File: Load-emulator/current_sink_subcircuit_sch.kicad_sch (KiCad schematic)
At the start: 3 parts, among them Q4 TIP41C, U4 AD8001AN

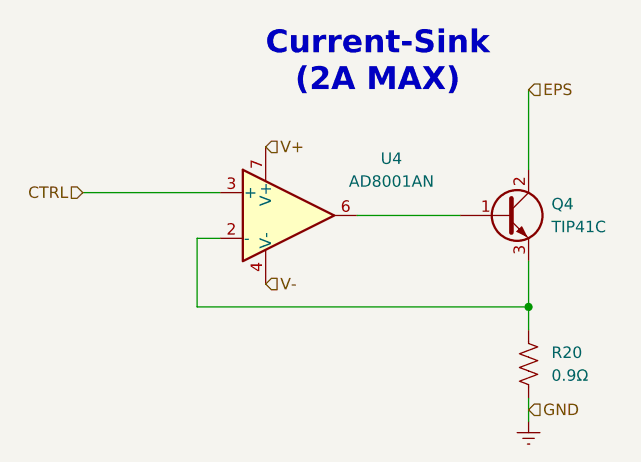
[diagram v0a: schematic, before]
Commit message: Replacement of the microcontroller w/ picoblade
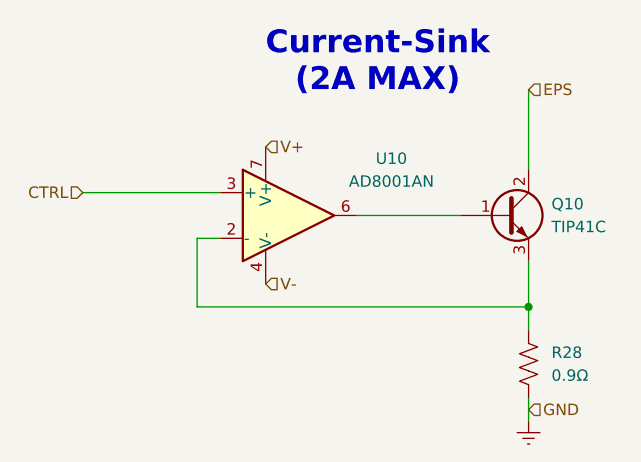
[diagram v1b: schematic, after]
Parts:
- renumbered Q4 to Q10, R20 to R28, U4 to U10
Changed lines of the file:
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@@
 		(dnp no)
 		(fields_autoplaced yes)
-		(property "Reference" "R20"
+		(property "Reference" "R28"
 			(at 167.64 105.4099 0)
 			(effects
@@
 				(path "/9054bfd2-3cc0-4c96-aa71-abdb09b76dc7/a12c045f-372a-4c5b-93d1-0c234b5f9c5c/87a0f9ee-fa92-48a0-98d1-72d297c3468c"
 					(reference "R21")
+					(unit 1)
+				)
+				(path "/9054bfd2-3cc0-4c96-aa71-abdb09b76dc7/a12c045f-372a-4c5b-93d1-0c234b5f9c5c/c40377b4-6929-4e4a-ac2d-4b484617f896"
+					(reference "R35")
 					(unit 1)
 				)
@@
 		(dnp no)
 		(fields_autoplaced yes)
-		(property "Reference" "#PWR033"
+		(property "Reference" "#PWR061"
 			(at 165.1 119.38 0)
 			(effects
@@
 				(path "/9054bfd2-3cc0-4c96-aa71-abdb09b76dc7/a12c045f-372a-4c5b-93d1-0c234b5f9c5c/87a0f9ee-fa92-48a0-98d1-72d297c3468c"
 					(reference "#PWR034")
+					(unit 1)
+				)
+				(path "/9054bfd2-3cc0-4c96-aa71-abdb09b76dc7/a12c045f-372a-4c5b-93d1-0c234b5f9c5c/c40377b4-6929-4e4a-ac2d-4b484617f896"
+					(reference "#PWR0101")
 					(unit 1)
 				)
@@
 		(dnp no)
 		(fields_autoplaced yes)
-		(property "Reference" "Q4"
+		(property "Reference" "Q10"
 			(at 167.64 88.8999 0)
 			(effects
@@
 				(path "/9054bfd2-3cc0-4c96-aa71-abdb09b76dc7/a12c045f-372a-4c5b-93d1-0c234b5f9c5c/87a0f9ee-fa92-48a0-98d1-72d297c3468c"
 					(reference "Q5")
+					(unit 1)
+				)
+				(path "/9054bfd2-3cc0-4c96-aa71-abdb09b76dc7/a12c045f-372a-4c5b-93d1-0c234b5f9c5c/c40377b4-6929-4e4a-ac2d-4b484617f896"
+					(reference "Q13")
 					(unit 1)
 				)
@@
 		(dnp no)
 		(fields_autoplaced yes)
-		(property "Reference" "U4"
+		(property "Reference" "U10"
 			(at 149.86 83.8514 0)
 			(effects
@@
 					(unit 1)
 				)
+				(path "/9054bfd2-3cc0-4c96-aa71-abdb09b76dc7/a12c045f-372a-4c5b-93d1-0c234b5f9c5c/c40377b4-6929-4e4a-ac2d-4b484617f896"
+					(reference "U13")
+					(unit 1)
+				)

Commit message: Added footprints for the remaining resistors, capacitors and ampops, as well as some 3D models
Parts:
- R28: footprint (none) -> Resistor_SMD:R_0201_0603Metric
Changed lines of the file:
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@@
 			)
 		)
-		(property "Footprint" ""
+		(property "Footprint" "Resistor_SMD:R_0201_0603Metric"
 			(at 166.116 106.934 90)
 			(effects

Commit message: Forgot to save files before last commit
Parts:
- removed U10: AD8001AN, Package_DIP:DIP-8_W7.62mm, symbol Amplifier_Operational:AD8001AN
- added U2: LM318H, LM318M:SOIC127P599X175-8N, symbol Amplifier_Operational:LM318H
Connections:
- net CTRL: now also U2.3 (+)
- net V+: now also U2.7 (V+)
- net V-: now also U2.4 (V-)
- net at Q10.3 (E), R28.1: now also U2.2 (-)
- net at Q10.1 (B): now also U2.6
- no-connect marks 0 -> 3
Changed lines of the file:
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@@
 		(color 0 0 0 0)
+	)
+	(no_connect
+		(at 138.43 97.79)
+	)
+	(no_connect
+		(at 138.43 82.55)
+	)
+	(no_connect
+		(at 140.97 97.79)
 	)
 	(wire
@@
 	(hierarchical_label "V+"
 		(shape input)
-		(at 135.89 82.55 0)
+		(at 135.89 82.55 90)
 		(fields_autoplaced yes)
 		(effects
@@
 	(hierarchical_label "V-"
 		(shape input)
-		(at 135.89 97.79 0)
+		(at 135.89 97.79 180)
 		(fields_autoplaced yes)
 		(effects
@@
 				(size 1.27 1.27)
 			)
-			(justify left)
+			(justify right)
 		)
 	)
@@
 	)
 	(symbol
-		(lib_id "Amplifier_Operational:AD8001AN")
+		(lib_id "Amplifier_Operational:LM318H")
 		(at 138.43 90.17 0)
 		(unit 1)
@@
 		(dnp no)
 		(fields_autoplaced yes)
-		(property "Reference" "U10"
-			(at 149.86 83.8514 0)
-			(effects
-				(font
-					(size 1.27 1.27)
-				)
-			)
-		)
-		(property "Value" "AD8001AN"
-			(at 149.86 86.3914 0)
-			(effects
-				(font
-					(size 1.27 1.27)
-				)
-			)
-		)
-		(property "Footprint" "Package_DIP:DIP-8_W7.62mm"
-			(at 135.89 95.25 0)
-			(effects
-				(font
-					(size 1.27 1.27)
-				)
-				(justify left)
-				(hide yes)
-			)
-		)
-		(property "Datasheet" "https://www.analog.com/media/en/technical-documentation/data-sheets/ad8001.pdf"
-			(at 142.24 86.36 0)
-			(effects
-				(font
-					(size 1.27 1.27)
-				)
-				(hide yes)
-			)
-		)
-		(property "Description" "Current Feedback Amplifier, 800 MHz, 50mW, DIP-8"
+		(property "Reference" "U2"
+			(at 148.59 83.8514 0)
+			(effects
+				(font
+					(size 1.27 1.27)
+				)
+			)
+		)
+		(property "Value" "LM318H"
+			(at 148.59 86.3914 0)
+			(effects
+				(font
+					(size 1.27 1.27)
+				)
+			)
+		)
+		(property "Footprint" "LM318M:SOIC127P599X175-8N"
 			(at 138.43 90.17 0)
 			(effects
@@
 			)
 		)
+		(property "Datasheet" "http://www.ti.com/lit/ds/symlink/lm318-n.pdf"
+			(at 138.43 90.17 0)
+			(effects
+				(font
+					(size 1.27 1.27)
+				)
+				(hide yes)
+			)
+		)
+		(property "Description" "Operational Amplifier, TO-99-8"
+			(at 138.43 90.17 0)
+			(effects
+				(font
+					(size 1.27 1.27)
+				)
+				(hide yes)
+			)
+		)
 		(pin "6"
 		)
+		(pin "5"
+		)
 		(pin "1"
 		)
+		(pin "4"
+		)
 		(pin "3"
 		)
+		(pin "2"
+		)
 		(pin "8"
 		)
-		(pin "5"
-		)
-		(pin "4"
-		)
 		(pin "7"
-		)
-		(pin "2"
 		)
 		(instances
 			(project "Load-emulator"
 				(path "/9054bfd2-3cc0-4c96-aa71-abdb09b76dc7/a12c045f-372a-4c5b-93d1-0c234b5f9c5c/128c0139-7aee-4d92-8032-2b2c6fcc70a3"
-					(reference "U10")
+					(reference "U7")
 					(unit 1)
 				)
 				(path "/9054bfd2-3cc0-4c96-aa71-abdb09b76dc7/a12c045f-372a-4c5b-93d1-0c234b5f9c5c/1c64d8a3-ab27-4c28-be0a-61e164321225"
-					(reference "U11")
+					(reference "U8")
 					(unit 1)
 				)
 				(path "/9054bfd2-3cc0-4c96-aa71-abdb09b76dc7/a12c045f-372a-4c5b-93d1-0c234b5f9c5c/29914013-a477-4717-a7a5-21a772c92b2e"
-					(reference "U8")
+					(reference "U6")
 					(unit 1)
 				)
 				(path "/9054bfd2-3cc0-4c96-aa71-abdb09b76dc7/a12c045f-372a-4c5b-93d1-0c234b5f9c5c/87a0f9ee-fa92-48a0-98d1-72d297c3468c"
+					(reference "U4")
+					(unit 1)
+				)
+				(path "/9054bfd2-3cc0-4c96-aa71-abdb09b76dc7/a12c045f-372a-4c5b-93d1-0c234b5f9c5c/c40377b4-6929-4e4a-ac2d-4b484617f896"
+					(reference "U2")
+					(unit 1)
+				)
+				(path "/9054bfd2-3cc0-4c96-aa71-abdb09b76dc7/a12c045f-372a-4c5b-93d1-0c234b5f9c5c/e0ddf382-1b56-45d3-a566-5cd39e11bb78"
+					(reference "U3")
+					(unit 1)
+				)
+				(path "/9054bfd2-3cc0-4c96-aa71-abdb09b76dc7/a12c045f-372a-4c5b-93d1-0c234b5f9c5c/ecd08cfa-ace2-4c26-a75b-4cdb3b0fd9bc"
 					(reference "U5")
 					(unit 1)
 				)
-				(path "/9054bfd2-3cc0-4c96-aa71-abdb09b76dc7/a12c045f-372a-4c5b-93d1-0c234b5f9c5c/c40377b4-6929-4e4a-ac2d-4b484617f896"
-					(reference "U13")
-					(unit 1)
-				)
-				(path "/9054bfd2-3cc0-4c96-aa71-abdb09b76dc7/a12c045f-372a-4c5b-93d1-0c234b5f9c5c/e0ddf382-1b56-45d3-a566-5cd39e11bb78"
-					(reference "U4")
-					(unit 1)
-				)
-				(path "/9054bfd2-3cc0-4c96-aa71-abdb09b76dc7/a12c045f-372a-4c5b-93d1-0c234b5f9c5c/ecd08cfa-ace2-4c26-a75b-4cdb3b0fd9bc"
-					(reference "U7")
-					(unit 1)
-				)

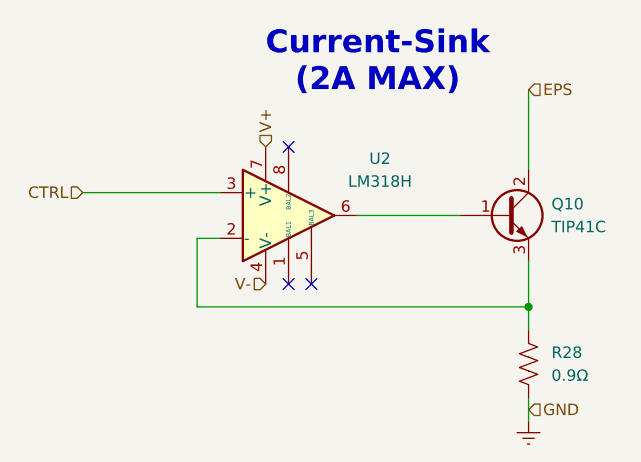
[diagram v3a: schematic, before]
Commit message: File with 3D models were created, because the models were previously saved at a local PC, so only one specific machine could load them; Better organization; EPS terminal labels were added to each current sink channel; Channels were searched for possible errors
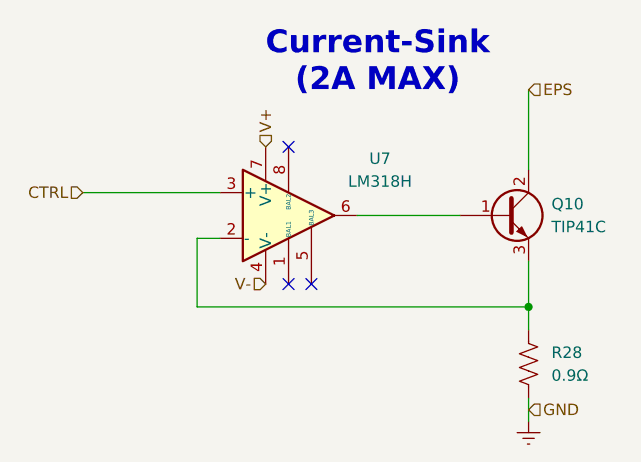
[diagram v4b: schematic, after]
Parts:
- renumbered U2 to U7
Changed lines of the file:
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@@
 		(dnp no)
 		(fields_autoplaced yes)
-		(property "Reference" "U2"
+		(property "Reference" "U7"
 			(at 148.59 83.8514 0)
 			(effects

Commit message: minor changes in connectors
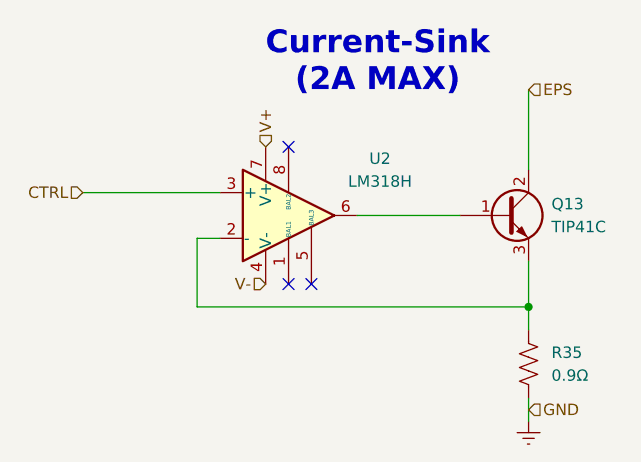
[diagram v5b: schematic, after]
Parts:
- renumbered Q10 to Q13, R28 to R35, U7 to U2
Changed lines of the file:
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@@
 (kicad_sch
-	(version 20231120)
+	(version 20250114)
 	(generator "eeschema")
-	(generator_version "8.0")
+	(generator_version "9.0")
 	(paper "A4")
+	(text "Current-Sink\n(2A MAX)\n"
+		(exclude_from_sim no)
+		(at 148.336 73.152 0)
+		(effects
+			(font
+				(size 2.54 2.54)
+				(thickness 0.254)
+				(bold yes)
+			)
+		)
+	)
 	(junction
 		(at 165.1 100.33)
@@
 		)
 	)
-	(text "Current-Sink\n(2A MAX)\n"
-		(exclude_from_sim no)
-		(at 148.336 73.152 0)
-		(effects
-			(font
-				(size 2.54 2.54)
-				(thickness 0.254)
-				(bold yes)
-			)
-		)
-	)
 	(hierarchical_label "V+"
 		(shape input)
 		(at 135.89 82.55 90)
-		(fields_autoplaced yes)
 		(effects
 			(font
@@
 		(shape input)
 		(at 165.1 76.2 0)
-		(fields_autoplaced yes)
 		(effects
 			(font
@@
 		(shape input)
 		(at 115.57 87.63 180)
-		(fields_autoplaced yes)
 		(effects
 			(font
@@
 		(shape input)
 		(at 135.89 97.79 180)
-		(fields_autoplaced yes)
 		(effects
 			(font
@@
 		(shape input)
 		(at 165.1 111.76 0)
-		(fields_autoplaced yes)
 		(effects
 			(font
@@
 		(dnp no)
 		(fields_autoplaced yes)
-		(property "Reference" "R28"
+		(property "Reference" "R35"
 			(at 167.64 105.4099 0)
 			(effects
@@
 		(dnp no)
 		(fields_autoplaced yes)
-		(property "Reference" "#PWR061"
+		(property "Reference" "#PWR0101"
 			(at 165.1 119.38 0)
 			(effects
@@
 		(dnp no)
 		(fields_autoplaced yes)
-		(property "Reference" "Q10"
+		(property "Reference" "Q13"
 			(at 167.64 88.8999 0)
 			(effects
@@
 		(dnp no)
 		(fields_autoplaced yes)
-		(property "Reference" "U7"
+		(property "Reference" "U2"
 			(at 148.59 83.8514 0)
 			(effects
